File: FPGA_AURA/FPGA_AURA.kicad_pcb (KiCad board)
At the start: 2 copper layers, 50 x 50 mm, 60 parts, among them J1 USB_C_Receptacle_USB2.0_16P, J101 XT30PW-M, U1 XC7A35T-2FTG256C, U2 W25Q256JVEIQ, U200 ADP5014, U201 NCP51200MNTXG, U3 FT232HQ-REEL, U500 MT41K128M16JT-125_IT_K

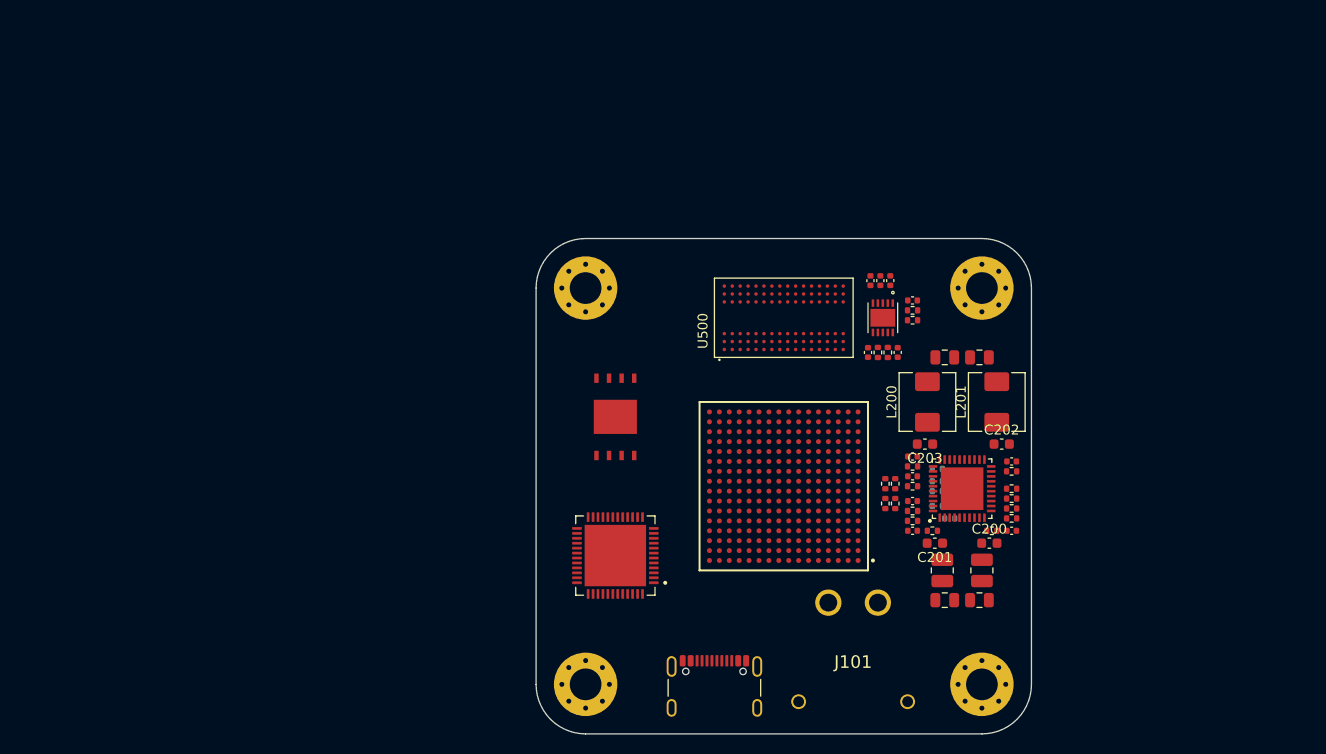
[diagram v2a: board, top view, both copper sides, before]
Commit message: Added USB power schottky and started DDR3L
Transferring from laptop to PC to decide DDR3 pins.
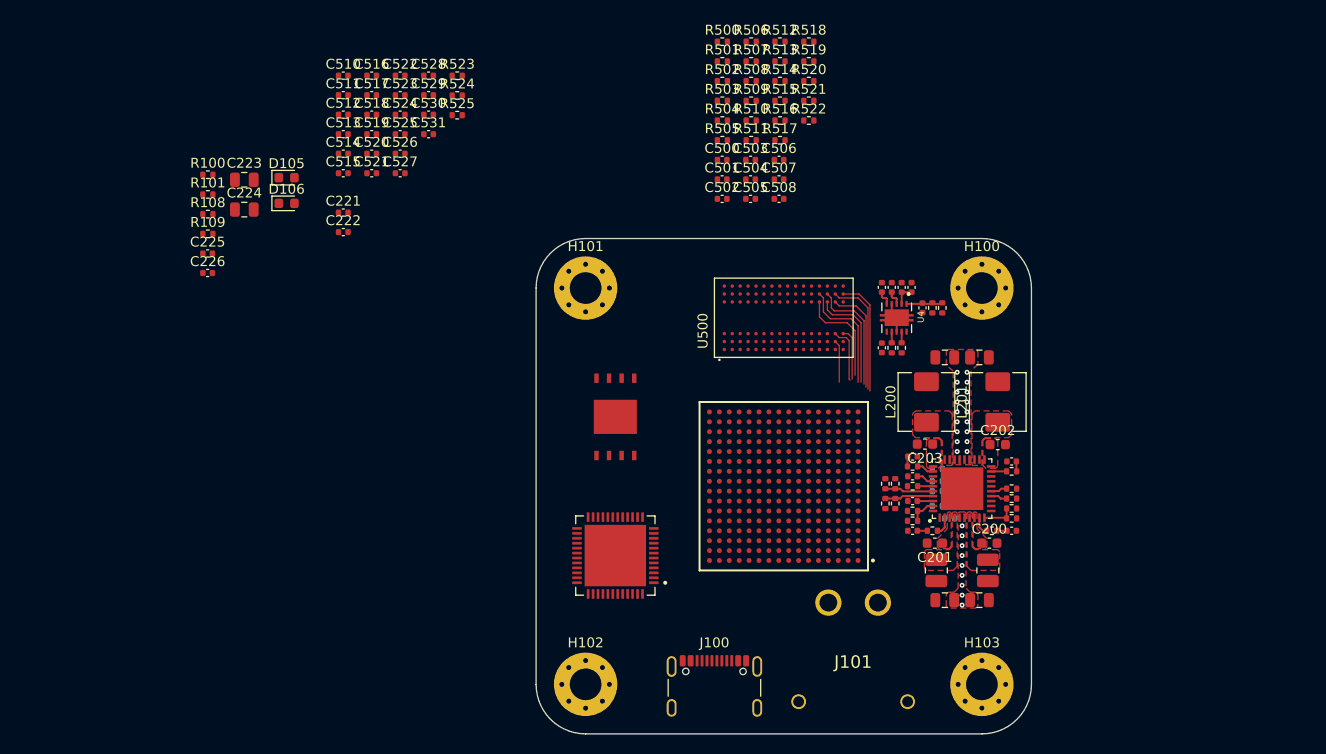
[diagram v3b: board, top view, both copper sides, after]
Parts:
- removed H1, H2, H3, H4: MountingHole_Pad, MountingHole:MountingHole_3.2mm_M3_Pad_Via
- removed J1: USB_C_Receptacle_USB2.0_16P, Connector_USB:USB_C_Receptacle_GCT_USB4105-xx-A_16P_TopMnt_Horizontal
- removed U201: NCP51200MNTXG, NCP51200MNTXG:SON50P300X300X100-11N
- added C221: 4u7, Capacitor_SMD:C_0402_1005Metric, F.Cu at (80.5, 47.4)
- added C222: 10u, Capacitor_SMD:C_0402_1005Metric, F.Cu at (80.5, 49.4)
- added C223: 47u, Capacitor_SMD:C_0805_2012Metric, F.Cu at (70.5, 44.1)
- added C224: 47u, Capacitor_SMD:C_0805_2012Metric, F.Cu at (70.5, 47.1)
- added C225: 100n, Capacitor_SMD:C_0402_1005Metric, F.Cu at (66.8, 51.5)
- added C226: 1u, Capacitor_SMD:C_0402_1005Metric, F.Cu at (66.8, 53.5)
- added C500: 100n, Capacitor_SMD:C_0402_1005Metric, F.Cu at (118.8, 42.1)
- added C501: 100n, Capacitor_SMD:C_0402_1005Metric, F.Cu at (118.8, 44.0)
- added C502: 100n, Capacitor_SMD:C_0402_1005Metric, F.Cu at (118.8, 46.0)
- added C503: 100n, Capacitor_SMD:C_0402_1005Metric, F.Cu at (121.7, 42.1)
- added C504: 100n, Capacitor_SMD:C_0402_1005Metric, F.Cu at (121.7, 44.0)
- added C505: 100n, Capacitor_SMD:C_0402_1005Metric, F.Cu at (121.7, 46.0)
- added C506: 100n, Capacitor_SMD:C_0402_1005Metric, F.Cu at (124.5, 42.1)
- added C507: 100n, Capacitor_SMD:C_0402_1005Metric, F.Cu at (124.5, 44.0)
- added C508: 10u, Capacitor_SMD:C_0402_1005Metric, F.Cu at (124.5, 46.0)
- added C510: 10n, Capacitor_SMD:C_0402_1005Metric, F.Cu at (80.5, 33.6)
- added C511: 10n, Capacitor_SMD:C_0402_1005Metric, F.Cu at (80.5, 35.5)
- added C512: 100n, Capacitor_SMD:C_0402_1005Metric, F.Cu at (80.5, 37.5)
- added C513: 100n, Capacitor_SMD:C_0402_1005Metric, F.Cu at (80.5, 39.5)
- added C514: 100n, Capacitor_SMD:C_0402_1005Metric, F.Cu at (80.5, 41.4)
- added C515: 100n, Capacitor_SMD:C_0402_1005Metric, F.Cu at (80.5, 43.4)
- added C516: 100n, Capacitor_SMD:C_0402_1005Metric, F.Cu at (83.4, 33.6)
- added C517: 100n, Capacitor_SMD:C_0402_1005Metric, F.Cu at (83.4, 35.5)
- added C518: 100n, Capacitor_SMD:C_0402_1005Metric, F.Cu at (83.4, 37.5)
- added C519: 100n, Capacitor_SMD:C_0402_1005Metric, F.Cu at (83.4, 39.5)
- added C520: 100n, Capacitor_SMD:C_0402_1005Metric, F.Cu at (83.4, 41.4)
- added C521: 100n, Capacitor_SMD:C_0402_1005Metric, F.Cu at (83.4, 43.4)
- added C522: 100n, Capacitor_SMD:C_0402_1005Metric, F.Cu at (86.3, 33.6)
- added C523: 100n, Capacitor_SMD:C_0402_1005Metric, F.Cu at (86.3, 35.5)
- added C524: 100n, Capacitor_SMD:C_0402_1005Metric, F.Cu at (86.3, 37.5)
- added C525: 100n, Capacitor_SMD:C_0402_1005Metric, F.Cu at (86.3, 39.5)
- added C526: 100n, Capacitor_SMD:C_0402_1005Metric, F.Cu at (86.3, 41.4)
- added C527: 100n, Capacitor_SMD:C_0402_1005Metric, F.Cu at (86.3, 43.4)
- added C528: 100n, Capacitor_SMD:C_0402_1005Metric, F.Cu at (89.2, 33.6)
- added C529: 100n, Capacitor_SMD:C_0402_1005Metric, F.Cu at (89.2, 35.5)
- added C530: 100n, Capacitor_SMD:C_0402_1005Metric, F.Cu at (89.2, 37.5)
- added C531: 100n, Capacitor_SMD:C_0402_1005Metric, F.Cu at (89.2, 39.5)
- added D105: LED, LED_SMD:LED_0603_1608Metric, F.Cu at (74.8, 43.9)
- added D106: LED, LED_SMD:LED_0603_1608Metric, F.Cu at (74.8, 46.5)
- added H100: MountingHole_Pad, MountingHole:MountingHole_3.2mm_M3_Pad_Via, F.Cu at (145.0, 55.0)
- added H101: MountingHole_Pad, MountingHole:MountingHole_3.2mm_M3_Pad_Via, F.Cu at (105.0, 55.0)
- added H102: MountingHole_Pad, MountingHole:MountingHole_3.2mm_M3_Pad_Via, F.Cu at (105.0, 95.0)
- added H103: MountingHole_Pad, MountingHole:MountingHole_3.2mm_M3_Pad_Via, F.Cu at (145.0, 95.0)
- added J100: USB_C_Receptacle_USB2.0_16P, Connector_USB:USB_C_Receptacle_GCT_USB4105-xx-A_16P_TopMnt_Horizontal, F.Cu at (118.0, 96.3)
- added R100: 5k1, Resistor_SMD:R_0402_1005Metric, F.Cu at (66.9, 43.6)
- added R101: 5k1, Resistor_SMD:R_0402_1005Metric, F.Cu at (66.9, 45.5)
- added R108: 1k, Resistor_SMD:R_0402_1005Metric, F.Cu at (66.9, 47.5)
- added R109: 1k, Resistor_SMD:R_0402_1005Metric, F.Cu at (66.9, 49.5)
- added R500: 40R2, Resistor_SMD:R_0402_1005Metric, F.Cu at (118.8, 30.1)
- added R501: 40R2, Resistor_SMD:R_0402_1005Metric, F.Cu at (118.8, 32.1)
- added R502: 40R2, Resistor_SMD:R_0402_1005Metric, F.Cu at (118.8, 34.1)
- added R503: 40R2, Resistor_SMD:R_0402_1005Metric, F.Cu at (118.8, 36.1)
- added R504: 40R2, Resistor_SMD:R_0402_1005Metric, F.Cu at (118.8, 38.1)
- added R505: 40R2, Resistor_SMD:R_0402_1005Metric, F.Cu at (118.8, 40.1)
- added R506: 40R2, Resistor_SMD:R_0402_1005Metric, F.Cu at (121.7, 30.1)
- added R507: 40R2, Resistor_SMD:R_0402_1005Metric, F.Cu at (121.7, 32.1)
- added R508: 40R2, Resistor_SMD:R_0402_1005Metric, F.Cu at (121.7, 34.1)
- added R509: 40R2, Resistor_SMD:R_0402_1005Metric, F.Cu at (121.7, 36.1)
- added R510: 40R2, Resistor_SMD:R_0402_1005Metric, F.Cu at (121.7, 38.1)
- added R511: 40R2, Resistor_SMD:R_0402_1005Metric, F.Cu at (121.7, 40.1)
- added R512: 40R2, Resistor_SMD:R_0402_1005Metric, F.Cu at (124.6, 30.1)
- added R513: 40R2, Resistor_SMD:R_0402_1005Metric, F.Cu at (124.6, 32.1)
- added R514: 40R2, Resistor_SMD:R_0402_1005Metric, F.Cu at (124.6, 34.1)
- added R515: 40R2, Resistor_SMD:R_0402_1005Metric, F.Cu at (124.6, 36.1)
- added R516: 40R2, Resistor_SMD:R_0402_1005Metric, F.Cu at (124.6, 38.1)
- added R517: 40R2, Resistor_SMD:R_0402_1005Metric, F.Cu at (124.6, 40.1)
- added R518: 40R2, Resistor_SMD:R_0402_1005Metric, F.Cu at (127.5, 30.1)
- added R519: 40R2, Resistor_SMD:R_0402_1005Metric, F.Cu at (127.5, 32.1)
- added R520: 40R2, Resistor_SMD:R_0402_1005Metric, F.Cu at (127.5, 34.1)
- added R521: 40R2, Resistor_SMD:R_0402_1005Metric, F.Cu at (127.5, 36.1)
- added R522: 81R, Resistor_SMD:R_0402_1005Metric, F.Cu at (127.5, 38.1)
- added R523: 240, Resistor_SMD:R_0402_1005Metric, F.Cu at (92.0, 33.6)
- added R524: 10k, Resistor_SMD:R_0402_1005Metric, F.Cu at (92.0, 35.6)
- added R525: 40R, Resistor_SMD:R_0402_1005Metric, F.Cu at (92.0, 37.5)
- added U4: TPS51200DRCR, TPS51200DRCR:VREG_V62_16624-01YE, F.Cu at (136.4, 58.0)
- C214: value 4u7 -> 100n
- C215: value 22u -> 10u
- C216: value 470n -> 1n
- C217: value 470n -> 10u
- C218: value 10n -> 10u
- C219: value 100n -> 10u
- R220: value 0R -> 10k
- R223: value 47k -> 10k
- moved C219 6.72 mm to (134.9, 54.9), turned to 90 degrees
- moved C216 5.93 mm to (139.0, 57.0), turned to -90 degrees
- moved C217 3.22 mm to (137.9, 54.9)
- moved R222 3.01 mm to (141.0, 57.0), turned to 90 degrees
- moved R221 2.36 mm to (140.0, 57.0), turned to -90 degrees
- moved C218 1.72 mm to (136.9, 54.9), turned to 90 degrees
- moved C214 1.67 mm to (134.9, 61.0)
- moved R220 1.48 mm to (135.9, 61.0)
- moved R223 1.48 mm to (136.9, 61.0)
- moved C215 0.70 mm to (135.9, 54.9)
- moved L202 0.60 mm to (140.4, 83.5)
- moved L203 0.60 mm to (145.6, 83.5)
- moved C202 0.40 mm to (146.6, 70.8)
- moved L200 0.10 mm to (139.4, 66.5)
- moved L201 0.10 mm to (146.6, 66.5)
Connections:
- C200 pad 1: +5V_FILT -> +5V
- C201 pad 1: +5V_FILT -> +5V
- C202 pad 1: +5V_FILT -> +5V
- C203 pad 1: +5V_FILT -> +5V
- C214 pad 1: +3V3 -> +VREF
- C215 pad 1: +1V35 -> +VTT
- C216 pad 1: +0V675 -> /200_Power_Regulation/TPS_REFIN
- C217 pad 1: +0V675 -> +1V35
- C218 pad 1: /200_Power_Regulation/VTT_VRI -> +1V35
- C219 pad 1: /200_Power_Regulation/VTT_VRO -> +VTT
- C220 pad 1: +5V_FILT -> +5V
- J101 pad 1: unconnected-(J101-Pad1) -> +5V
- J101 pad 2: unconnected-(J101-Pad2) -> GND
- J101 pad 3: unconnected-(J101-Pad3) -> GND
- J101 pad 4: unconnected-(J101-Pad4) -> GND
- R200 pad 1: +5V_FILT -> +5V
- R220 pad 2: /200_Power_Regulation/VTT_EN -> Net-(U4-EN)
- R221 pad 1: +1V35 -> /200_Power_Regulation/TPS_REFIN
- R221 pad 2: /200_Power_Regulation/VTT_VRI -> GND
- R222 pad 1: /200_Power_Regulation/VTT_VRI -> +1V35
- R222 pad 2: GND -> /200_Power_Regulation/TPS_REFIN
- R223 pad 2: VTT_PG -> DDR_PGOOD
- U1 pad A6: +3V3 -> +1V35
- U1 pad B3: +3V3 -> +1V35
- U1 pad D7: +3V3 -> +1V35
- U1 pad E4: +3V3 -> +1V35
- U1 pad F1: +3V3 -> +1V35
- U1 pad J2: +3V3 -> +1V35
- U200 pad 17: +5V_FILT -> +5V
- U200 pad 20: +5V_FILT -> +5V
- U200 pad 21: +5V_FILT -> +5V
- U200 pad 3: +5V_FILT -> +5V
- U200 pad 30: +5V_FILT -> +5V
- U200 pad 31: +5V_FILT -> +5V
- U200 pad 34: +5V_FILT -> +5V
- U200 pad 8: +5V_FILT -> +5V
- U500 pad A1: VDDQ -> +1V35
- U500 pad A2: unconnected-(U500-DQ13-PadA2) -> DDR3_DQ13
- U500 pad A3: unconnected-(U500-DQ15-PadA3) -> DDR3_DQ15
- U500 pad A7: unconnected-(U500-DQ12-PadA7) -> DDR3_DQ12
- U500 pad A8: VDDQ -> +1V35
- U500 pad A9: Net-(U500-VSS-PadA9) -> GND
- U500 pad B1: Net-(U500-VSSQ-PadB1) -> GND
- U500 pad B2: VDD -> +1V35
- U500 pad B3: Net-(U500-VSS-PadA9) -> GND
- U500 pad B7: unconnected-(U500-~{UDQS}-PadB7) -> DDR3_DQS1-
- U500 pad B8: unconnected-(U500-DQ14-PadB8) -> DDR3_DQ14
- U500 pad B9: Net-(U500-VSSQ-PadB1) -> GND
- U500 pad C1: VDDQ -> +1V35
- U500 pad C2: unconnected-(U500-DQ11-PadC2) -> DDR3_DQ11
- U500 pad C3: unconnected-(U500-DQ9-PadC3) -> DDR3_DQ9
- U500 pad C7: unconnected-(U500-UDQS-PadC7) -> DDR3_DQS1+
- U500 pad C8: unconnected-(U500-DQ10-PadC8) -> DDR3_DQ10
- U500 pad C9: VDDQ -> +1V35
- U500 pad D1: Net-(U500-VSSQ-PadB1) -> GND
- U500 pad D2: VDDQ -> +1V35
- U500 pad D3: unconnected-(U500-UDM-PadD3) -> DDR3_DM1
- U500 pad D7: unconnected-(U500-DQ8-PadD7) -> DDR3_DQ8
- U500 pad D8: Net-(U500-VSSQ-PadB1) -> GND
- U500 pad D9: VDD -> +1V35
- U500 pad E1: Net-(U500-VSS-PadA9) -> GND
- U500 pad E2: Net-(U500-VSSQ-PadB1) -> GND
- U500 pad E3: unconnected-(U500-DQ0-PadE3) -> DDR3_DQ0
- U500 pad E7: unconnected-(U500-LDM-PadE7) -> DDR3_DM0
- U500 pad E8: Net-(U500-VSSQ-PadB1) -> GND
- U500 pad E9: VDDQ -> +1V35
- U500 pad F1: VDDQ -> +1V35
- U500 pad F2: unconnected-(U500-DQ2-PadF2) -> DDR3_DQ2
- U500 pad F3: unconnected-(U500-LDQS-PadF3) -> DDR3_DQS0+
- U500 pad F7: unconnected-(U500-DQ1-PadF7) -> DDR3_DQ1
- U500 pad F8: unconnected-(U500-DQ3-PadF8) -> DDR3_DQ3
- U500 pad F9: Net-(U500-VSSQ-PadB1) -> GND
- U500 pad G1: Net-(U500-VSSQ-PadB1) -> GND
- U500 pad G2: unconnected-(U500-DQ6-PadG2) -> DDR3_DQ6
- U500 pad G3: unconnected-(U500-~{LDQS}-PadG3) -> DDR3_DQS0-
- U500 pad G7: VDD -> +1V35
- U500 pad G8: Net-(U500-VSS-PadA9) -> GND
- U500 pad G9: Net-(U500-VSSQ-PadB1) -> GND
- U500 pad H1: unconnected-(U500-VREFDQ-PadH1) -> +VREF
- U500 pad H2: VDDQ -> +1V35
- U500 pad H3: unconnected-(U500-DQ4-PadH3) -> DDR3_DQ4
- U500 pad H7: unconnected-(U500-DQ7-PadH7) -> DDR3_DQ7
- U500 pad H8: unconnected-(U500-DQ5-PadH8) -> DDR3_DQ5
- U500 pad H9: VDDQ -> +1V35
- U500 pad J2: Net-(U500-VSS-PadA9) -> GND
- U500 pad J3: unconnected-(U500-~{RAS}-PadJ3) -> DDR3_RAS
- U500 pad J7: unconnected-(U500-CK-PadJ7) -> DDR3_CK+
- U500 pad J8: Net-(U500-VSS-PadA9) -> GND
- U500 pad K1: unconnected-(U500-ODT-PadK1) -> DDR3_ODT
- U500 pad K2: VDD -> +1V35
- U500 pad K3: unconnected-(U500-~{CAS}-PadK3) -> DDR3_CAS
- U500 pad K7: unconnected-(U500-~{CK}-PadK7) -> DDR3_CK-
- U500 pad K8: VDD -> +1V35
- U500 pad K9: unconnected-(U500-CKE-PadK9) -> DDR3_CKE
- U500 pad L2: unconnected-(U500-~{CS}-PadL2) -> DDR3_CS
- U500 pad L3: unconnected-(U500-~{WE}-PadL3) -> DDR3_WE
- U500 pad L7: unconnected-(U500-A10/AP-PadL7) -> DDR3_A10
- U500 pad L8: unconnected-(U500-ZQ-PadL8) -> /500_DDR3L/DDR3_ZQ
- U500 pad M1: Net-(U500-VSS-PadA9) -> GND
- U500 pad M2: unconnected-(U500-BA0-PadM2) -> DDR3_BA0
- U500 pad M3: unconnected-(U500-BA2-PadM3) -> DDR3_BA2
- U500 pad M8: unconnected-(U500-VREFCA-PadM8) -> +VREF
- U500 pad M9: Net-(U500-VSS-PadA9) -> GND
- U500 pad N1: VDD -> +1V35
- U500 pad N2: unconnected-(U500-A3-PadN2) -> DDR3_A3
- U500 pad N3: unconnected-(U500-A0-PadN3) -> DDR3_A0
- U500 pad N7: unconnected-(U500-A12/~{BC}-PadN7) -> DDR3_A12
- U500 pad N8: unconnected-(U500-BA1-PadN8) -> DDR3_BA1
- U500 pad N9: VDD -> +1V35
- U500 pad P1: Net-(U500-VSS-PadA9) -> GND
- U500 pad P2: unconnected-(U500-A5-PadP2) -> DDR3_A5
- U500 pad P3: unconnected-(U500-A2-PadP3) -> DDR3_A2
- U500 pad P7: unconnected-(U500-A1-PadP7) -> DDR3_A1
- U500 pad P8: unconnected-(U500-A4-PadP8) -> DDR3_A4
- U500 pad P9: Net-(U500-VSS-PadA9) -> GND
- U500 pad R1: VDD -> +1V35
- U500 pad R2: unconnected-(U500-A7-PadR2) -> DDR3_A7
- U500 pad R3: unconnected-(U500-A9-PadR3) -> DDR3_A9
- U500 pad R7: unconnected-(U500-A11-PadR7) -> DDR3_A11
- U500 pad R8: unconnected-(U500-A6-PadR8) -> DDR3_A6
- U500 pad R9: VDD -> +1V35
- U500 pad T1: Net-(U500-VSS-PadA9) -> GND
- U500 pad T2: unconnected-(U500-~{RESET}-PadT2) -> DDR3_RESET
- U500 pad T3: unconnected-(U500-A13-PadT3) -> DDR3_A13
- U500 pad T8: unconnected-(U500-A8-PadT8) -> DDR3_A8
- U500 pad T9: Net-(U500-VSS-PadA9) -> GND
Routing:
- net DDR3_A6: track 0.00 -> 12.1 mm
- net DDR3_A8: track 0.00 -> 11.9 mm
- net DDR3_A4: track 0.00 -> 11.8 mm
- net DDR3_BA1: track 0.00 -> 11.8 mm
- net DDR3_A11: track 0.00 -> 10.9 mm
- net DDR3_A1: track 0.00 -> 10.7 mm
- net DDR3_A12: track 0.00 -> 10.2 mm
- net DDR3_A9: track 0.00 -> 5.73 mm
- net DDR3_A13: track 0.00 -> 5.27 mm
- net /200_Power_Regulation/ADP_1V0_PD: track 0.00 -> 4.93 mm
- net /200_Power_Regulation/ADP_1V8_PD: track 0.00 -> 4.92 mm
- net DDR3_A7: track 0.00 -> 4.27 mm
- net /200_Power_Regulation/TPS_REFIN: track 0.00 -> 3.80 mm
- net /200_Power_Regulation/ADP_FB4: track 0.00 -> 3.27 mm
- net +VTT: track 0.00 -> 3.14 mm
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- added copper zone on F.Cu, net +5V
- added copper zone on F.Cu, net /200_Power_Regulation/ADP_SW1
- added copper zone on F.Cu, net /200_Power_Regulation/ADP_SW2
- added copper zone on F.Cu, net /200_Power_Regulation/ADP_SW3
- added copper zone on F.Cu, net /200_Power_Regulation/ADP_SW4
- added copper zone on F.Cu, net GND
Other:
- copper layers 2 -> 6

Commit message: Moving progress to laptop.
Started to decide on BGA fanout for DDR. Next is for the FPGA and to assign byte lanes to DQ.
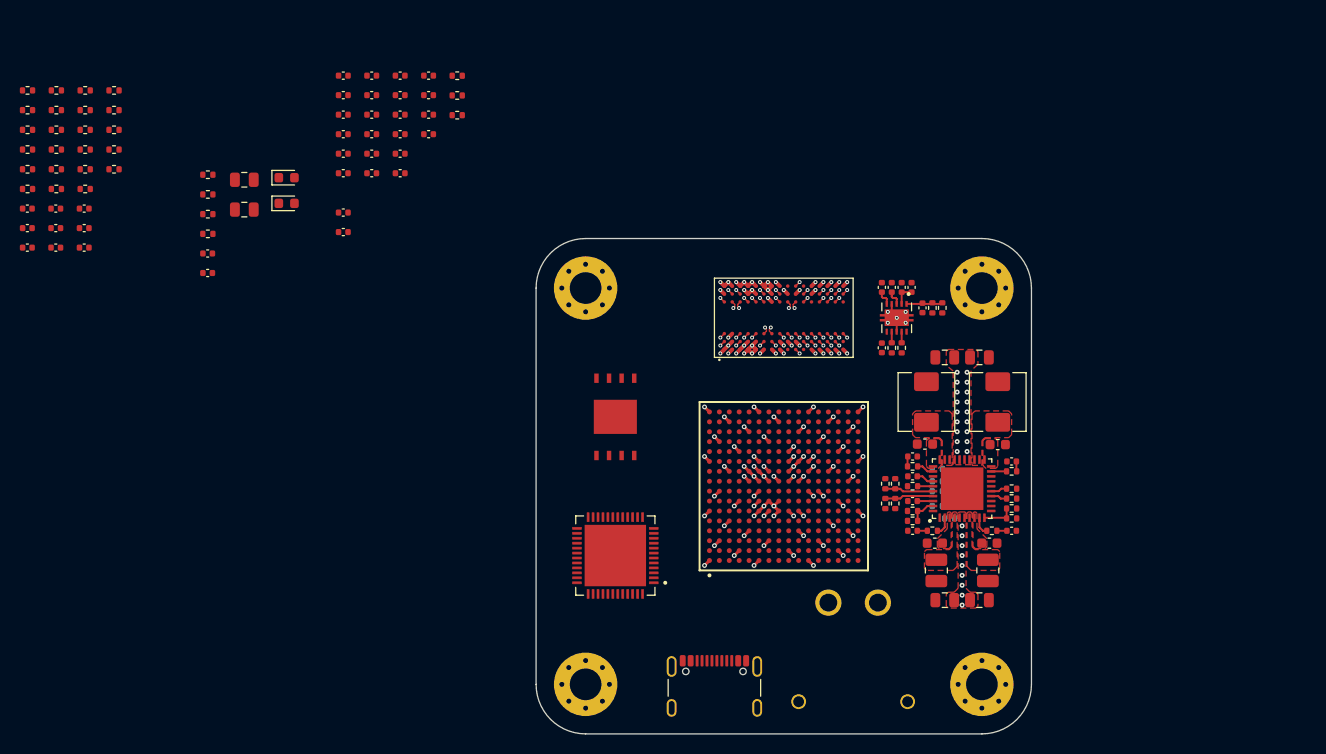
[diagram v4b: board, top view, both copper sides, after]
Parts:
- moved C500 70.3 mm to (48.6, 47.0)
- moved C501 70.3 mm to (48.6, 49.0)
- moved C502 70.3 mm to (48.6, 50.9)
- moved C503 70.3 mm to (51.5, 47.0)
- moved C504 70.3 mm to (51.5, 49.0)
- moved C505 70.3 mm to (51.5, 50.9)
- moved C506 70.3 mm to (54.4, 47.0)
- moved C507 70.3 mm to (54.4, 49.0)
- moved C508 70.3 mm to (54.4, 50.9)
- moved R500 70.3 mm to (48.7, 35.0)
- moved R501 70.3 mm to (48.7, 37.0)
- moved R502 70.3 mm to (48.7, 39.0)
- moved R503 70.3 mm to (48.7, 41.0)
- moved R504 70.3 mm to (48.7, 43.0)
- moved R505 70.3 mm to (48.7, 45.0)
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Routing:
- net DDR3_CK-: track 0.00 -> 54.3 mm, vias 0 -> 1
- net DDR3_CK+: track 0.00 -> 52.8 mm, vias 0 -> 1
- net GND: track 3.01 -> 50.1 mm, vias 27 -> 86
- net DDR3_DQS1-: track 0.00 -> 20.8 mm, vias 0 -> 1
- net DDR3_DQS1+: track 0.00 -> 20.7 mm, vias 0 -> 1
- net +1V35: track 2.19 -> 18.9 mm, vias 0 -> 24
- net DDR3_DQ10: track 0.00 -> 13.1 mm, vias 0 -> 1
- net DDR3_DQ8: track 0.00 -> 12.9 mm, vias 0 -> 1
- net DDR3_DQ14: track 0.00 -> 12.8 mm, vias 0 -> 1
- net DDR3_DQ12: track 0.00 -> 12.5 mm, vias 0 -> 1
- net DDR3_A6: track 12.1 -> 0.57 mm, vias 0 -> 1
- net DDR3_A0: track 0.00 -> 11.5 mm, vias 0 -> 1
- net DDR3_A8: track 11.9 -> 0.57 mm, vias 0 -> 1
- net DDR3_A4: track 11.8 -> 0.57 mm, vias 0 -> 1
- net DDR3_BA1: track 11.8 -> 0.57 mm, vias 0 -> 1
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- added copper zone on In1.Cu, net GND
- added copper zone on In3.Cu, net GND

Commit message: Moving to PC.
Placed the VTT termination resistors roughly, rotated the DDR IC 180, and deleted the initial draft of routing.
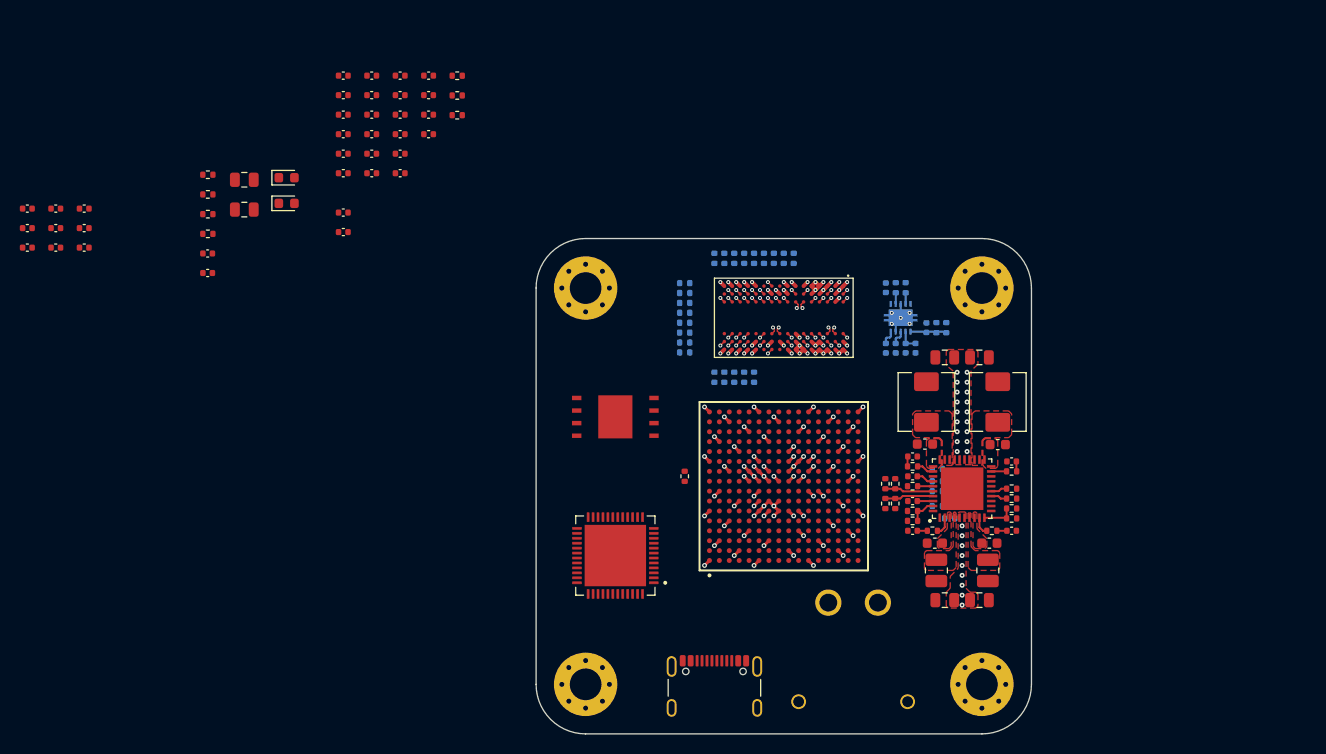
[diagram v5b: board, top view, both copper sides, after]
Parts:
- C214, C215, C216, C217, C218, C219, R220, R221, R222, R223, R500, R501, R502, R503, R504, R505, R506, R507, R508, R509, R510, R511, R512, R513, R514, R515, R516, R517, R518, R519, R520, R521, U4: moved to B.Cu
- moved R507 72.6 mm to (119.0, 64.0), turned to 90 degrees
- moved R509 72.2 mm to (120.0, 64.0), turned to 90 degrees
- moved R505 71.9 mm to (118.0, 64.0), turned to 90 degrees
- moved R500 71.4 mm to (118.0, 52.0), turned to -90 degrees
- moved R515 70.4 mm to (121.0, 64.0), turned to 90 degrees
- moved R519 70.2 mm to (126.0, 52.0), turned to -90 degrees
- moved R517 70.1 mm to (122.0, 64.0), turned to 90 degrees
- moved R502 70.0 mm to (115.0, 61.5)
- moved R501 70.0 mm to (115.0, 59.5)
- moved R510 70.0 mm to (121.0, 52.0), turned to -90 degrees
- moved R514 69.7 mm to (123.0, 52.0), turned to -90 degrees
- moved R508 69.6 mm to (120.0, 52.0), turned to -90 degrees
- moved R506 69.5 mm to (119.0, 52.0), turned to -90 degrees
- moved R513 69.1 mm to (122.0, 52.0), turned to -90 degrees
- moved R520 68.8 mm to (125.0, 52.0), turned to -90 degrees
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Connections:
- U1 pad A16: +3V3 -> +1V35
- U1 pad A6: +1V35 -> +3V3
- U1 pad B13: +3V3 -> +1V35
- U1 pad B3: +1V35 -> +3V3
- U1 pad C10: +3V3 -> +1V35
- U1 pad D7: +1V35 -> +3V3
- U1 pad E14: +3V3 -> +1V35
- U1 pad E4: +1V35 -> +3V3
- U1 pad F1: +1V35 -> +3V3
- U1 pad H15: +3V3 -> +1V35
- U1 pad J12: +3V3 -> +1V35
- U1 pad J2: +1V35 -> +3V3
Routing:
- net DDR3_CK-: track 54.3 -> 0.78 mm
- net DDR3_CK+: track 52.8 -> 0.78 mm
- net DDR3_DQS1-: track 20.8 -> 0.78 mm
- net DDR3_DQS1+: track 20.7 -> 0.78 mm
- net DDR3_DQ10: track 13.1 -> 0.57 mm
- net DDR3_DQ8: track 12.9 -> 0.57 mm
- net DDR3_DQ14: track 12.8 -> 0.57 mm
- net DDR3_DQ12: track 12.5 -> 0.57 mm
- net DDR3_A0: track 11.5 -> 0.57 mm
- net DDR3_BA2: track 10.5 -> 0.57 mm
- net DDR3_DQ7: track 10.4 -> 0.57 mm
- net DDR3_DQ1: track 10.4 -> 0.57 mm
- net DDR3_A2: track 9.34 -> 0.57 mm
- net DDR3_DQS0-: track 8.36 -> 0.78 mm
- net DDR3_DQS0+: track 8.36 -> 0.78 mm
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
